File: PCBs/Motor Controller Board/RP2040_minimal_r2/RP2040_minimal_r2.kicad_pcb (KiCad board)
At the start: 2 copper layers, 52 x 51 mm, 34 parts, among them J1 USB_B_Micro, J2 Conn_01x02, J3 Conn_02x18_Odd_Even, J4 Conn_02x18_Odd_Even, U1 NCP1117-3.3_SOT223, U2 W25Q128JVS, U3 RP2040, Y1 ABM8-272-T3

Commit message: vault backup: 2025-04-08 00:30:09
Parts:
- added BTSEL1: SW_Push, Button_Switch_THT:KSA_Tactile_SPST, F.Cu at (42.9, 92.3)
- added C18: 0.1u, Capacitor_SMD:C_0603_1608Metric_Pad1.08x0.95mm_HandSolder, F.Cu at (38.8, 74.4)
- added C19: 10u, Capacitor_SMD:CP_Elec_5x5.4, F.Cu at (54.8, 76.6)
- added C20: 0.1u, Capacitor_SMD:C_0603_1608Metric_Pad1.08x0.95mm_HandSolder, F.Cu at (38.8, 76.9)
- added C21: 10u, Capacitor_SMD:CP_Elec_5x5.4, F.Cu at (54.8, 83.4)
- added D1: LED, LED_SMD:LED_0603_1608Metric_Pad1.05x0.95mm_HandSolder, F.Cu at (61.5, 74.4)
- added D2: LED, LED_SMD:LED_0603_1608Metric_Pad1.05x0.95mm_HandSolder, F.Cu at (61.5, 77.0)
- added J5: Conn_01x06_Pin, Connector_PinHeader_2.54mm:PinHeader_1x06_P2.54mm_Vertical, F.Cu at (43.3, 75.5)
- added J6: Conn_01x02, Connector_AMASS:AMASS_XT30U-M_1x02_P5.0mm_Vertical, F.Cu at (53.9, 90.5)
- added J7: Conn_01x06_Pin, Connector_PinHeader_2.54mm:PinHeader_1x06_P2.54mm_Vertical, F.Cu at (48.0, 75.5)
- added R10: 430, Resistor_SMD:R_0603_1608Metric_Pad0.98x0.95mm_HandSolder, F.Cu at (38.8, 89.5)
- added R11: 430, Resistor_SMD:R_0603_1608Metric_Pad0.98x0.95mm_HandSolder, F.Cu at (38.8, 92.0)
- added R6: R, Resistor_SMD:R_0603_1608Metric_Pad0.98x0.95mm_HandSolder, F.Cu at (38.8, 79.4)
- added R7: 2k, Resistor_SMD:R_0603_1608Metric_Pad0.98x0.95mm_HandSolder, F.Cu at (38.8, 81.9)
- added R8: 2k, Resistor_SMD:R_0603_1608Metric_Pad0.98x0.95mm_HandSolder, F.Cu at (38.8, 84.4)
- added R9: R, Resistor_SMD:R_0603_1608Metric_Pad0.98x0.95mm_HandSolder, F.Cu at (38.8, 87.0)
- added U4: DRV8245HQRXZRQ1, footprints:RXZ0016A-MFG, F.Cu at (53.6, 98.1)
- added U5: DRV8245HQRXZRQ1, footprints:RXZ0016A-MFG, F.Cu at (59.5, 98.1)
- C1, C17, C4: footprint Capacitor_SMD:C_0805_2012Metric -> Capacitor_SMD:C_0603_1608Metric_Pad1.08x0.95mm_HandSolder
- C10, C11, C12, C13, C14, C15, C16, C2, C3, C5, C6, C7, C8, C9: footprint Capacitor_SMD:C_0402_1005Metric -> Capacitor_SMD:C_0603_1608Metric_Pad1.08x0.95mm_HandSolder
- H1, H2, H3, H4: footprint MountingHole:MountingHole_2.7mm_M2.5 -> MountingHole:MountingHole_3.2mm_M3_DIN965_Pad_TopBottom
- moved J3 65.0 mm to (11.0, 69.9)
- moved J4 31.0 mm to (152.6, 72.7)
- moved H3 23.0 mm to (135.0, 126.5)
- moved H4 23.0 mm to (65.0, 126.5)
- moved H1 21.0 mm to (65.0, 74.0)
- moved H2 21.0 mm to (135.0, 74.0)
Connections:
- J3 pad 28: /GPIO12 -> +3V3
- J4 pad 25: /GPIO17 -> +3V3
- U3 pad 15: /GPIO12 -> +3V3
- U3 pad 28: /GPIO17 -> +3V3
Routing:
- net +3V3: track 42.6 -> 82.5 mm
- net /GPIO12: track 20.5 -> 0.00 mm
- net /GPIO17: track 19.4 -> 0.00 mm
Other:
- board size 52 x 51 mm -> 80.9 x 62 mm

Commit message: PCB Work
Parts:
- removed J3, J4: Conn_02x18_Odd_Even, Connector_PinHeader_2.54mm:PinHeader_2x18_P2.54mm_Vertical
- BTSEL1: footprint Button_Switch_THT:KSA_Tactile_SPST -> Button_Switch_THT:SW_PUSH-12mm
- R1, R2, R3, R4, R5: footprint Resistor_SMD:R_0402_1005Metric -> Resistor_SMD:R_0603_1608Metric_Pad0.98x0.95mm_HandSolder
- moved J7 94.1 mm to (122.9, 132.4), turned to -90 degrees
- moved C18 86.4 mm to (111.4, 121.4), turned to -90 degrees
- moved R9 86.3 mm to (119.4, 117.9), turned to -90 degrees
- moved R10 76.9 mm to (113.5, 107.8), turned to 180 degrees
- moved R11 76.0 mm to (114.5, 99.0), turned to 180 degrees
- moved R8 74.1 mm to (108.0, 111.0)
- moved C20 69.0 mm to (91.6, 121.4), turned to -90 degrees
- moved J5 65.2 mm to (75.2, 132.4), turned to 90 degrees
- moved U5 65.0 mm to (119.0, 124.2)
- moved C21 64.8 mm to (105.6, 123.6), turned to 90 degrees
- moved C19 64.0 mm to (98.1, 123.7), turned to 90 degrees
- moved J6 61.1 mm to (97.4, 133.4)
- moved D1 57.6 mm to (110.5, 104.8), turned to 180 degrees
- moved R6 57.5 mm to (82.7, 116.6), turned to -90 degrees
- moved R7 55.1 mm to (80.0, 118.5)
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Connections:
- BTSEL1 pad 2: /USB_BOOT -> /~{USB_BOOT}
- J5 pad 1: /GPIO7 -> /GPIO8
- J5 pad 2: /GPIO6 -> /GPIO9
- J7 pad 1: /GPIO9 -> /GPIO6
- J7 pad 2: /GPIO8 -> /GPIO7
- R7 pad 2: +3V3 -> /GPIO12
- R8 pad 2: +3V3 -> /GPIO17
- U3 pad 15: +3V3 -> /GPIO12
- U3 pad 28: +3V3 -> /GPIO17
- U4 pad 1: +3V3 -> /GPIO12
- U4 pad 10: /GPIO11 -> /GPIO15
- U4 pad 11: /GPIO13 -> /GPIO14
- U4 pad 12: /GPIO14 -> /GPIO13
- U5 pad 1: +3V3 -> /GPIO17
- U5 pad 10: /GPIO16 -> /GPIO20
- U5 pad 11: /GPIO18 -> /GPIO19
- U5 pad 12: /GPIO19 -> /GPIO18
- U5 pad 3: /GPIO15 -> /GPIO16
- U5 pad 5: Net-(J7-Pin_5) -> Net-(J7-Pin_6)
- U5 pad 6: Net-(J7-Pin_5) -> Net-(J7-Pin_6)
- U5 pad 8: Net-(J7-Pin_6) -> Net-(J7-Pin_5)
- U5 pad 9: Net-(J7-Pin_6) -> Net-(J7-Pin_5)
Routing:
- net +3V3: track 82.5 -> 202.2 mm
- net /GPIO6: track 22.0 -> 99.6 mm
- net GND: track 29.7 -> 105.5 mm, vias 22 -> 72
- net /GPIO7: track 20.8 -> 95.6 mm
- net VM: track 0.00 -> 51.4 mm
- net /GPIO29_ADC3: track 33.2 -> 0.00 mm
- net /GPIO0: track 31.8 -> 0.00 mm
- net /GPIO12: track 0.00 -> 31.7 mm
- net /GPIO28_ADC2: track 31.6 -> 0.00 mm
- net /GPIO1: track 30.2 -> 0.00 mm
- net /GPIO27_ADC1: track 29.9 -> 0.00 mm
- net /GPIO2: track 28.5 -> 0.00 mm
- net /GPIO26_ADC0: track 28.3 -> 0.00 mm
- net Net-(J7-Pin_5): track 0.00 -> 27.5 mm
- net /GPIO3: track 26.9 -> 0.00 mm
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- added copper zone on F.Cu, net VM
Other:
- board size 80.9 x 62 mm -> 72.5 x 69 mm
- board text removed: "GP0"
- board text removed: "GP1"
- board text removed: "GP10"
- board text removed: "GP11"
- board text removed: "GP12"
- board text removed: "GP13"
- board text removed: "GP14"
- board text removed: "GP15"
- board text removed: "GP16"
- board text removed: "GP17"
- board text removed: "GP18"
- board text removed: "GP19"
- board text removed: "GP2"
- board text removed: "GP20"
- board text removed: "GP21"
- board text removed: "GP22"
- board text removed: "GP23"
- board text removed: "GP24"
- board text removed: "GP25"
- board text removed: "GP26"
- board text removed: "GP27"
- board text removed: "GP28"
- board text removed: "GP29"
- board text removed: "GP3"
- board text removed: "GP4"
- board text removed: "GP5"
- board text removed: "GP6"
- board text removed: "GP7"
- board text removed: "GP8"
- board text removed: "GP9"
- board text removed: "RUN"
- board text removed: "SWCLK"
- board text removed: "SWD"

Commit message: Oop, I forgor to push
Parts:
- added J4: Conn_01x07, Connector_PinSocket_2.54mm:PinSocket_1x07_P2.54mm_Vertical, F.Cu at (131.9, 110.1)
- added J8: Conn_01x06, Connector_PinHeader_2.54mm:PinHeader_1x06_P2.54mm_Vertical, F.Cu at (65.7, 97.2)
- moved C15 3.70 mm to (111.2, 93.7), turned to 90 degrees
- moved C16 2.13 mm to (109.0, 93.7), turned to 90 degrees
- moved C11 1.89 mm to (92.5, 95.4)
- moved D2 1.08 mm to (111.1, 99.9)
- moved R11 1.08 mm to (115.1, 99.9)
- moved C7 1.05 mm to (102.5, 106.6)
- moved C4 1.05 mm to (111.6, 89.5)
- moved R5 0.56 mm to (98.8, 106.8)
- moved C14 0.35 mm to (100.7, 106.7)
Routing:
- net /GPIO5: track 0.00 -> 35.0 mm
- net /GPIO4: track 0.00 -> 34.0 mm
- net /GPIO23: track 0.00 -> 33.7 mm
- net /GPIO3: track 0.00 -> 33.1 mm
- net /GPIO24: track 0.00 -> 32.8 mm
- net /GPIO2: track 0.00 -> 32.2 mm
- net /GPIO25: track 0.00 -> 31.9 mm
- net /GPIO1: track 0.00 -> 31.3 mm
- net /GPIO26_ADC0: track 0.00 -> 30.9 mm
- net /GPIO0: track 0.00 -> 30.8 mm
- net /GPIO27_ADC1: track 0.00 -> 30.0 mm
- net /GPIO29_ADC3: track 0.00 -> 29.7 mm
- net /GPIO28_ADC2: track 0.00 -> 29.2 mm
- net +3V3: track 202.2 -> 226.8 mm
- net +1V1: track 18.4 -> 26.1 mm
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
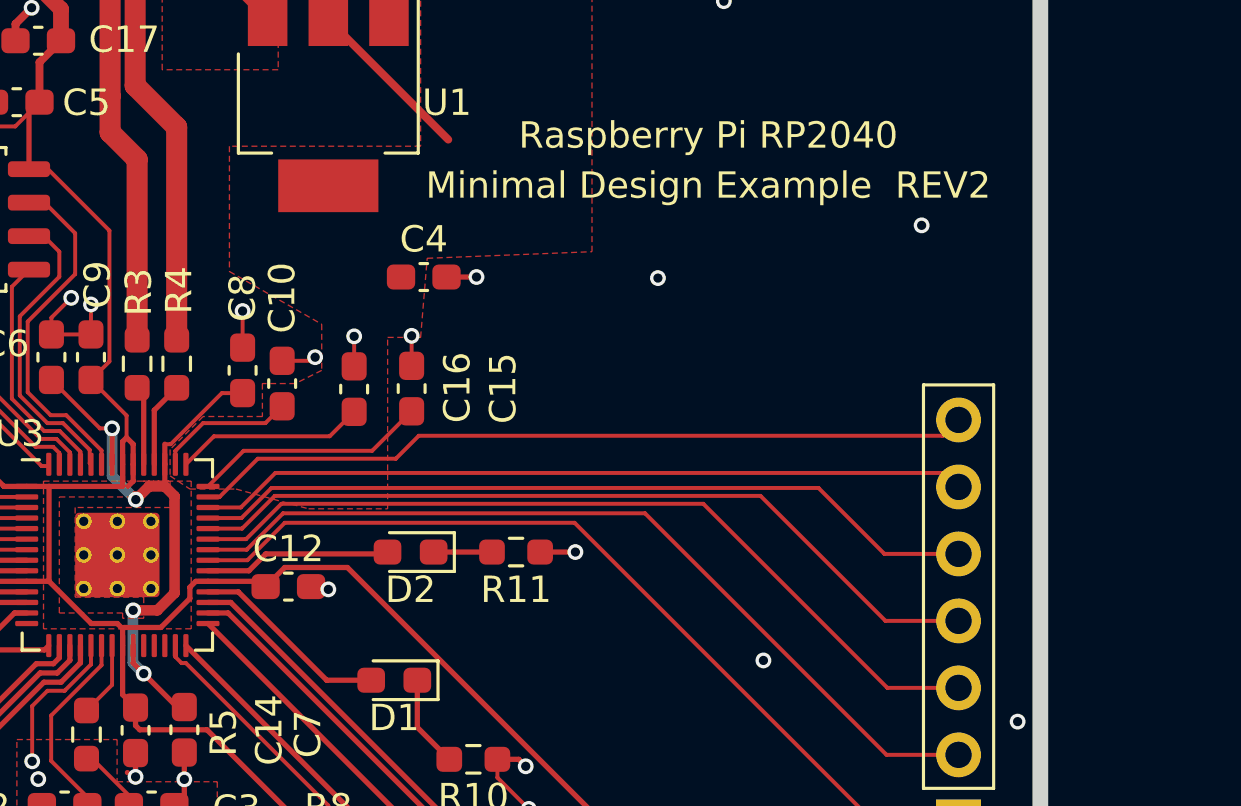
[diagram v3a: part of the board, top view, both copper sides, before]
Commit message: RUN tied high
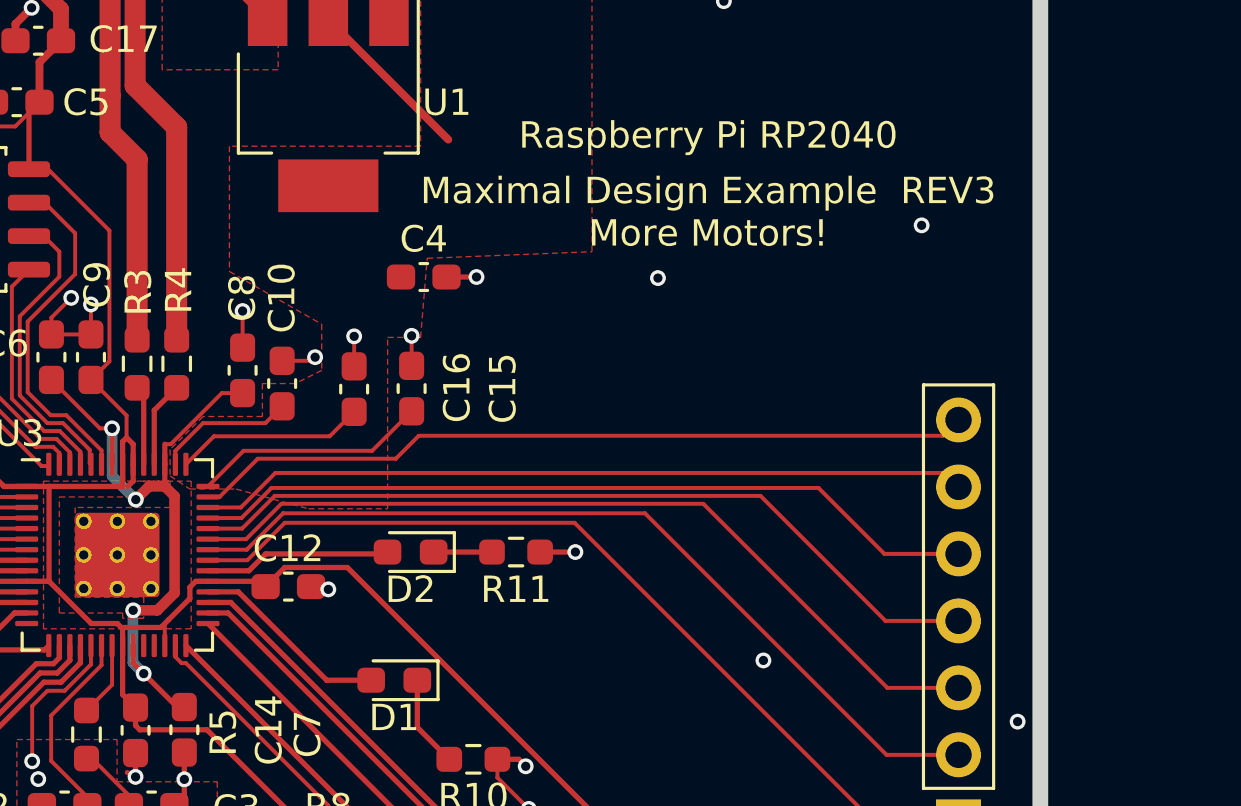
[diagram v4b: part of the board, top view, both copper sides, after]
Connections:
- U3 pad 26: /RUN -> +3V3
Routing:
- net +3V3: track 226.8 -> 227.9 mm
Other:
- board text added: "Maximal Design Example REV3 More Motors!"
- board text removed: "Minimal Design Example REV2"
